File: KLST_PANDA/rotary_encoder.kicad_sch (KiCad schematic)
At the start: 10 parts, among them SW4 ENCODER

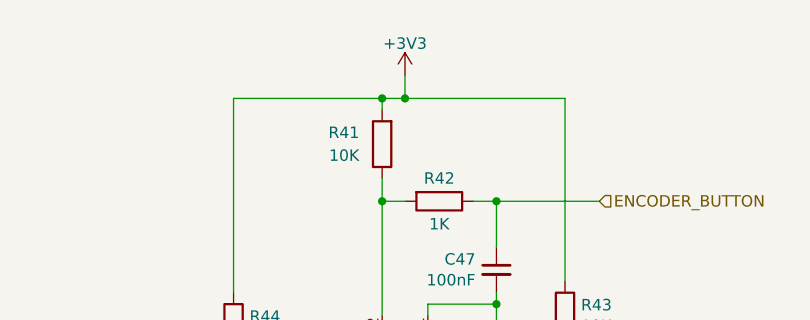
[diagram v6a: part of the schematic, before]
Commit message: removed DRC warnings and error, added power page
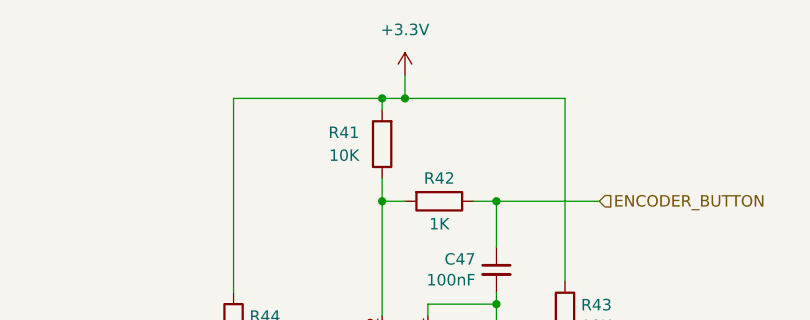
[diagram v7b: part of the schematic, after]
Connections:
- net +3V3 renamed +3.3V
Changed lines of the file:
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@@
         )
         (path "/b4513875-4c57-4720-bcc5-43ead67fe18f/b123f5e9-cc72-42aa-83b5-20f52795babc/87cd59e0-a7cb-4402-bde3-1e8396956bda"
-          (reference "#PWR058") (unit 1)
-        )
-        (path "/b4513875-4c57-4720-bcc5-43ead67fe18f/b123f5e9-cc72-42aa-83b5-20f52795babc/ed61e32f-240e-4d2b-b2a8-d00b0710740e"
-          (reference "#PWR060") (unit 1)
+          (reference "#PWR053") (unit 1)
+        )
+        (path "/b4513875-4c57-4720-bcc5-43ead67fe18f/b123f5e9-cc72-42aa-83b5-20f52795babc/ed61e32f-240e-4d2b-b2a8-d00b0710740e"
+          (reference "#PWR055") (unit 1)
         )
       )
@@
         )
         (path "/b4513875-4c57-4720-bcc5-43ead67fe18f/b123f5e9-cc72-42aa-83b5-20f52795babc/87cd59e0-a7cb-4402-bde3-1e8396956bda"
-          (reference "R38") (unit 1)
-        )
-        (path "/b4513875-4c57-4720-bcc5-43ead67fe18f/b123f5e9-cc72-42aa-83b5-20f52795babc/ed61e32f-240e-4d2b-b2a8-d00b0710740e"
-          (reference "R44") (unit 1)
+          (reference "R24") (unit 1)
+        )
+        (path "/b4513875-4c57-4720-bcc5-43ead67fe18f/b123f5e9-cc72-42aa-83b5-20f52795babc/ed61e32f-240e-4d2b-b2a8-d00b0710740e"
+          (reference "R30") (unit 1)
         )
       )
@@
         )
         (path "/b4513875-4c57-4720-bcc5-43ead67fe18f/b123f5e9-cc72-42aa-83b5-20f52795babc/87cd59e0-a7cb-4402-bde3-1e8396956bda"
-          (reference "R41") (unit 1)
-        )
-        (path "/b4513875-4c57-4720-bcc5-43ead67fe18f/b123f5e9-cc72-42aa-83b5-20f52795babc/ed61e32f-240e-4d2b-b2a8-d00b0710740e"
-          (reference "R47") (unit 1)
+          (reference "R27") (unit 1)
+        )
+        (path "/b4513875-4c57-4720-bcc5-43ead67fe18f/b123f5e9-cc72-42aa-83b5-20f52795babc/ed61e32f-240e-4d2b-b2a8-d00b0710740e"
+          (reference "R33") (unit 1)
         )
       )
@@
         )
         (path "/b4513875-4c57-4720-bcc5-43ead67fe18f/b123f5e9-cc72-42aa-83b5-20f52795babc/87cd59e0-a7cb-4402-bde3-1e8396956bda"
-          (reference "R40") (unit 1)
-        )
-        (path "/b4513875-4c57-4720-bcc5-43ead67fe18f/b123f5e9-cc72-42aa-83b5-20f52795babc/ed61e32f-240e-4d2b-b2a8-d00b0710740e"
-          (reference "R46") (unit 1)
+          (reference "R26") (unit 1)
+        )
+        (path "/b4513875-4c57-4720-bcc5-43ead67fe18f/b123f5e9-cc72-42aa-83b5-20f52795babc/ed61e32f-240e-4d2b-b2a8-d00b0710740e"
+          (reference "R32") (unit 1)
+        )
+      )
+    )
+  )
+  (symbol (lib_id "power:+3.3V") (at 149.86 71.12 0) (unit 1)
+    (in_bom yes) (on_board yes) (dnp no) (fields_autoplaced)
+    (property "Reference" "#PWR077" (at 149.86 74.93 0)
+      (effects (font (size 1.27 1.27)) hide)
+    )
+    (property "Value" "+3.3V" (at 149.86 66.04 0)
+      (effects (font (size 1.27 1.27)))
+    )
+    (property "Footprint" "" (at 149.86 71.12 0)
+      (effects (font (size 1.27 1.27)) hide)
+    )
+    (property "Datasheet" "" (at 149.86 71.12 0)
+      (effects (font (size 1.27 1.27)) hide)
+    )
+    (pin "1")
+    (instances
+      (project "KLST_PANDA"
+        (path "/b4513875-4c57-4720-bcc5-43ead67fe18f/47e8e77e-c64e-4c44-bfd8-2073580a3d85"
+          (reference "#PWR077") (unit 1)
+        )
+        (path "/b4513875-4c57-4720-bcc5-43ead67fe18f/b123f5e9-cc72-42aa-83b5-20f52795babc/87cd59e0-a7cb-4402-bde3-1e8396956bda"
+          (reference "#PWR052") (unit 1)
+        )
+        (path "/b4513875-4c57-4720-bcc5-43ead67fe18f/b123f5e9-cc72-42aa-83b5-20f52795babc/ed61e32f-240e-4d2b-b2a8-d00b0710740e"
+          (reference "#PWR054") (unit 1)
         )
       )
@@
         )
         (path "/b4513875-4c57-4720-bcc5-43ead67fe18f/b123f5e9-cc72-42aa-83b5-20f52795babc/87cd59e0-a7cb-4402-bde3-1e8396956bda"
-          (reference "R36") (unit 1)
-        )
-        (path "/b4513875-4c57-4720-bcc5-43ead67fe18f/b123f5e9-cc72-42aa-83b5-20f52795babc/ed61e32f-240e-4d2b-b2a8-d00b0710740e"
-          (reference "R42") (unit 1)
+          (reference "R22") (unit 1)
+        )
+        (path "/b4513875-4c57-4720-bcc5-43ead67fe18f/b123f5e9-cc72-42aa-83b5-20f52795babc/ed61e32f-240e-4d2b-b2a8-d00b0710740e"
+          (reference "R28") (unit 1)
         )
       )
@@
         )
         (path "/b4513875-4c57-4720-bcc5-43ead67fe18f/b123f5e9-cc72-42aa-83b5-20f52795babc/87cd59e0-a7cb-4402-bde3-1e8396956bda"
-          (reference "C61") (unit 1)
-        )
-        (path "/b4513875-4c57-4720-bcc5-43ead67fe18f/b123f5e9-cc72-42aa-83b5-20f52795babc/ed61e32f-240e-4d2b-b2a8-d00b0710740e"
-          (reference "C64") (unit 1)
+          (reference "C37") (unit 1)
+        )
+        (path "/b4513875-4c57-4720-bcc5-43ead67fe18f/b123f5e9-cc72-42aa-83b5-20f52795babc/ed61e32f-240e-4d2b-b2a8-d00b0710740e"
+          (reference "C40") (unit 1)
         )
       )
@@
         )
         (path "/b4513875-4c57-4720-bcc5-43ead67fe18f/b123f5e9-cc72-42aa-83b5-20f52795babc/87cd59e0-a7cb-4402-bde3-1e8396956bda"
-          (reference "R37") (unit 1)
-        )
-        (path "/b4513875-4c57-4720-bcc5-43ead67fe18f/b123f5e9-cc72-42aa-83b5-20f52795babc/ed61e32f-240e-4d2b-b2a8-d00b0710740e"
-          (reference "R43") (unit 1)
+          (reference "R23") (unit 1)
+        )
+        (path "/b4513875-4c57-4720-bcc5-43ead67fe18f/b123f5e9-cc72-42aa-83b5-20f52795babc/ed61e32f-240e-4d2b-b2a8-d00b0710740e"
+          (reference "R29") (unit 1)
         )
       )
@@
         )
         (path "/b4513875-4c57-4720-bcc5-43ead67fe18f/b123f5e9-cc72-42aa-83b5-20f52795babc/87cd59e0-a7cb-4402-bde3-1e8396956bda"
-          (reference "C62") (unit 1)
-        )
-        (path "/b4513875-4c57-4720-bcc5-43ead67fe18f/b123f5e9-cc72-42aa-83b5-20f52795babc/ed61e32f-240e-4d2b-b2a8-d00b0710740e"
-          (reference "C65") (unit 1)
+          (reference "C38") (unit 1)
+        )
+        (path "/b4513875-4c57-4720-bcc5-43ead67fe18f/b123f5e9-cc72-42aa-83b5-20f52795babc/ed61e32f-240e-4d2b-b2a8-d00b0710740e"
+          (reference "C41") (unit 1)
         )
       )
@@
         )
         (path "/b4513875-4c57-4720-bcc5-43ead67fe18f/b123f5e9-cc72-42aa-83b5-20f52795babc/87cd59e0-a7cb-4402-bde3-1e8396956bda"
-          (reference "R39") (unit 1)
-        )
-        (path "/b4513875-4c57-4720-bcc5-43ead67fe18f/b123f5e9-cc72-42aa-83b5-20f52795babc/ed61e32f-240e-4d2b-b2a8-d00b0710740e"
-          (reference "R45") (unit 1)
+          (reference "R25") (unit 1)
+        )
+        (path "/b4513875-4c57-4720-bcc5-43ead67fe18f/b123f5e9-cc72-42aa-83b5-20f52795babc/ed61e32f-240e-4d2b-b2a8-d00b0710740e"
+          (reference "R31") (unit 1)
         )
       )
@@
         )
         (path "/b4513875-4c57-4720-bcc5-43ead67fe18f/b123f5e9-cc72-42aa-83b5-20f52795babc/87cd59e0-a7cb-4402-bde3-1e8396956bda"
-          (reference "C60") (unit 1)
-        )
-        (path "/b4513875-4c57-4720-bcc5-43ead67fe18f/b123f5e9-cc72-42aa-83b5-20f52795babc/ed61e32f-240e-4d2b-b2a8-d00b0710740e"
-          (reference "C63") (unit 1)
-        )
-      )
-    )
-  )
-  (symbol (lib_id "power:+3V3") (at 149.86 71.12 0) (unit 1)
-    (in_bom yes) (on_board yes) (dnp no)
-    (property "Reference" "#PWR066" (at 149.86 74.93 0)
-      (effects (font (size 1.27 1.27)) hide)
-    )
-    (property "Value" "+3V3" (at 149.86 67.564 0)
-      (effects (font (size 1.27 1.27)))
-    )
-    (property "Footprint" "" (at 149.86 71.12 0)
-      (effects (font (size 1.27 1.27)) hide)
-    )
-    (property "Datasheet" "" (at 149.86 71.12 0)
-      (effects (font (size 1.27 1.27)) hide)
-    )
-    (pin "1")
-    (instances
-      (project "KLST_SHEEP"
-        (path "/7c1fd6fc-5c53-4ccb-a456-46fe6fc0bc71/00000000-0000-0000-0000-000060628872"
-          (reference "#PWR066") (unit 1)
-        )
-        (path "/7c1fd6fc-5c53-4ccb-a456-46fe6fc0bc71/00000000-0000-0000-0000-00006075a95b"
-          (reference "#PWR068") (unit 1)
-        )
-      )
-      (project "KLST_PANDA"
-        (path "/b4513875-4c57-4720-bcc5-43ead67fe18f/b123f5e9-cc72-42aa-83b5-20f52795babc"
-          (reference "#PWR?") (unit 1)
-        )
-        (path "/b4513875-4c57-4720-bcc5-43ead67fe18f/b123f5e9-cc72-42aa-83b5-20f52795babc/87cd59e0-a7cb-4402-bde3-1e8396956bda"
-          (reference "#PWR057") (unit 1)
-        )
-        (path "/b4513875-4c57-4720-bcc5-43ead67fe18f/b123f5e9-cc72-42aa-83b5-20f52795babc/ed61e32f-240e-4d2b-b2a8-d00b0710740e"
-          (reference "#PWR059") (unit 1)
-        )
-      )
+          (reference "C36") (unit 1)
+        )
+        (path "/b4513875-4c57-4720-bcc5-43ead67fe18f/b123f5e9-cc72-42aa-83b5-20f52795babc/ed61e32f-240e-4d2b-b2a8-d00b0710740e"
+          (reference "C39") (unit 1)
+        )
+      )
